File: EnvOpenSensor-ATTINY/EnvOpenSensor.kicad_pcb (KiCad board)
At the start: 2 copper layers, 89.7 x 67.5 mm, 347 parts, among them IC1 IS31FL3730-QFLS2-TR, IC2 IS31FL3730-QFLS2-TR, IC3 IS31FL3730-QFLS2-TR, IC4 IS31FL3730-QFLS2-TR, J1 HRO_TYPE-C-31-M-12, J3 AVR-ISP-6, SW1 SW_Push, SW2 SW_Push, SW3 SW_Push, SW4 SW_Push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

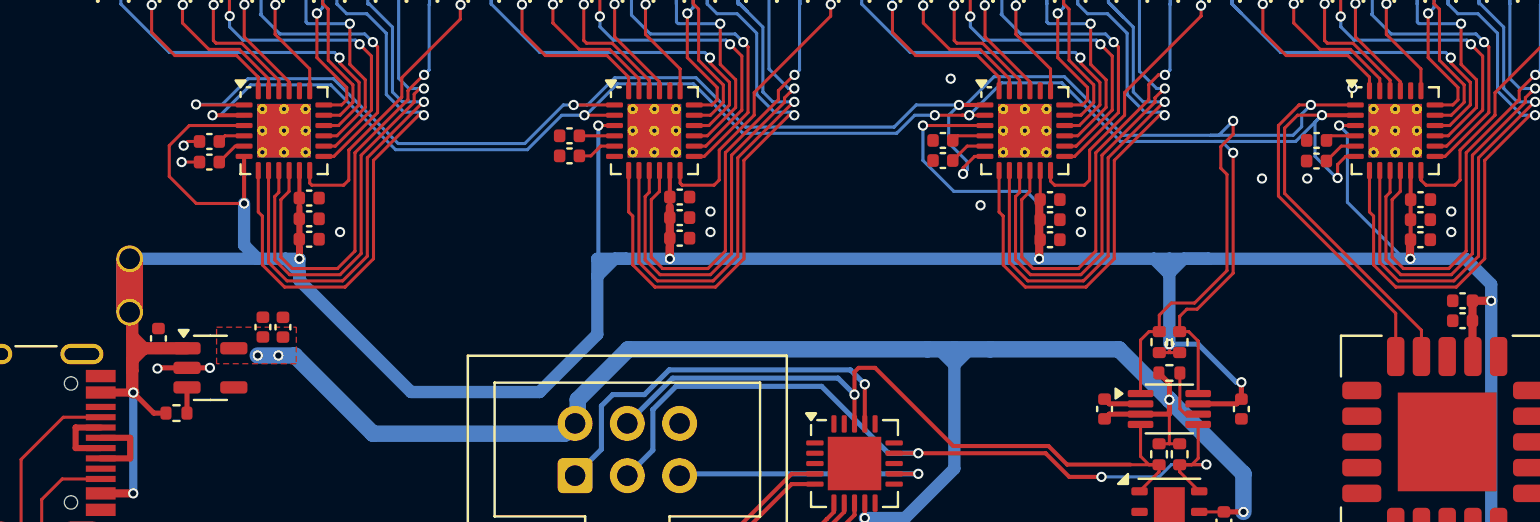
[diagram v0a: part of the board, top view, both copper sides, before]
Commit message: made a few corrections to duplicated vias and trace routing
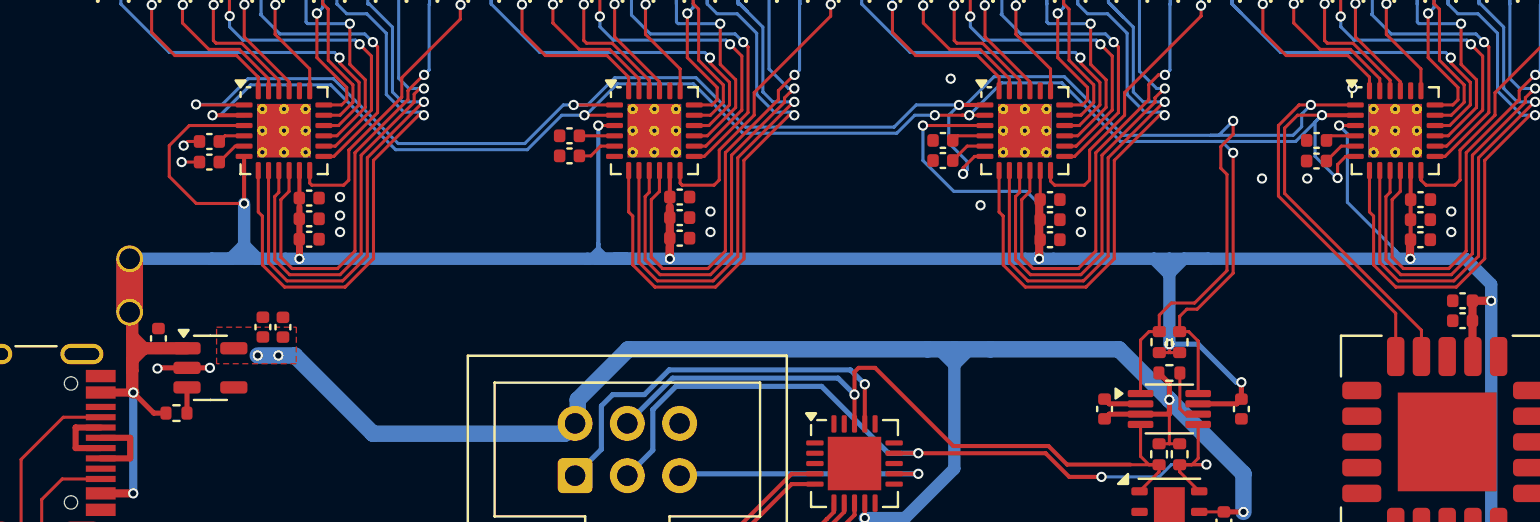
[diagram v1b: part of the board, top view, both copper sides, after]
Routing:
- net VCC: track 181.9 -> 179.5 mm
- net GND: vias 18 -> 20
